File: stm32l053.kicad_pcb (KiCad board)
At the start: 2 copper layers, 29 x 64.5 mm, 5 parts, among them P1 CONN_01X25, P2 CONN_01X25, U1 STM32_LQFP64

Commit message: Restart layout
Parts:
- added C3: 100nF, Capacitors_SMD:C_0805_HandSoldering, B.Cu at (151.8, 116.8)
- added C4: 10uF, Capacitors_SMD:C_0805_HandSoldering, F.Cu at (148.6, 94.0)
- added P3: CONN_01X23, Pin_Headers:Pin_Header_Straight_1x23, F.Cu at (162.6, 81.3)
- added P4: BOOT_MODE, Pin_Headers:Pin_Header_Straight_1x02, F.Cu at (142.2, 81.3)
- added P5: Ext Xtal, Resistors_SMD:R_0805_HandSoldering, F.Cu at (158.8, 110.5)
- added R1: 10K, Resistors_SMD:R_0805_HandSoldering, F.Cu at (174.0, 91.4)
- added R2: 0, Resistors_SMD:R_0805_HandSoldering, F.Cu at (189.2, 100.3)
- added R3: 0, Resistors_SMD:R_0805_HandSoldering, F.Cu at (189.2, 108.0)
- added SW1: SW_PUSH, Buttons_Switches_SMD:SW_SPST_B3U-1000P, F.Cu at (154.9, 81.3)
- C1: moved to B.Cu
- C2: value 100nF -> C
- P1: value CONN_01X25 -> SWD; footprint Pin_Headers:Pin_Header_Straight_1x25 -> Pin_Headers:Pin_Header_Straight_1x06
- P2: value CONN_01X25 -> CONN_01X23; footprint Pin_Headers:Pin_Header_Straight_1x25 -> Pin_Headers:Pin_Header_Straight_1x23
- moved P1 56.2 mm to (143.5, 137.2), turned to 90 degrees
- moved P2 25.4 mm to (137.2, 81.3)
- moved C1 11.8 mm to (148.3, 116.8), turned to 270 degrees
- moved C2 6.52 mm to (142.7, 108.1)
- moved U1 1.27 mm to (149.9, 118.1), turned to 225 degrees
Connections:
- C2 pad 1: VDDA -> Net-(C2-Pad1)
- P1 pad 2: Net-(P1-Pad2) -> SWCLK
- P1 pad 3: Net-(P1-Pad3) -> Earth
- P1 pad 4: Net-(P1-Pad4) -> SWDIO
- P1 pad 5: Net-(P1-Pad5) -> NRST
- P1 pad 6: Net-(P1-Pad6) -> SWO
- P2 pad 1: Net-(P2-Pad1) -> VDD
- P2 pad 10: Net-(P2-Pad10) -> /PA8
- P2 pad 11: Net-(P2-Pad11) -> /PA9
- P2 pad 12: Net-(P2-Pad12) -> /PA10
- P2 pad 13: Net-(P2-Pad13) -> /PA11
- P2 pad 14: Net-(P2-Pad14) -> /PA12
- P2 pad 15: Net-(P2-Pad15) -> /PA15
- P2 pad 16: Net-(P2-Pad16) -> /PC0
- P2 pad 17: Net-(P2-Pad17) -> /PC1
- P2 pad 18: Net-(P2-Pad18) -> /PC2
- P2 pad 19: Net-(P2-Pad19) -> /PC3
- P2 pad 2: Net-(P2-Pad2) -> /PA0
- P2 pad 20: Net-(P2-Pad20) -> /PC4
- P2 pad 21: Net-(P2-Pad21) -> /PC5
- P2 pad 22: Net-(P2-Pad22) -> /PC6
- P2 pad 23: Net-(P2-Pad23) -> Earth
- P2 pad 3: Net-(P2-Pad3) -> /PA1
- P2 pad 4: Net-(P2-Pad4) -> /PA2
- P2 pad 5: Net-(P2-Pad5) -> /PA3
- P2 pad 6: Net-(P2-Pad6) -> /PA4
- P2 pad 7: Net-(P2-Pad7) -> /PA5
- P2 pad 8: Net-(P2-Pad8) -> /PA6
- P2 pad 9: Net-(P2-Pad9) -> /PA7
- U1 pad 1: (no net) -> Net-(C3-Pad2)
- U1 pad 10: Net-(P1-Pad20) -> /PC2
- U1 pad 11: Net-(P1-Pad21) -> /PC3
- U1 pad 12: (no net) -> Earth
- U1 pad 13: VDDA -> VDD
- U1 pad 14: Net-(P1-Pad2) -> /PA0
- U1 pad 15: Net-(P1-Pad3) -> /PA1
- U1 pad 16: Net-(P1-Pad4) -> /PA2
- U1 pad 17: Net-(P1-Pad5) -> /PA3
- U1 pad 18: (no net) -> Earth
- U1 pad 2: Net-(P2-Pad22) -> /PC13
- U1 pad 20: Net-(P1-Pad6) -> /PA4
- U1 pad 21: Net-(P1-Pad7) -> /PA5
- U1 pad 22: Net-(P1-Pad8) -> /PA6
- U1 pad 23: Net-(P1-Pad9) -> /PA7
- U1 pad 24: Net-(P1-Pad22) -> /PC4
- U1 pad 25: Net-(P1-Pad23) -> /PC5
- U1 pad 26: Net-(P2-Pad1) -> /PB0
- U1 pad 27: Net-(P2-Pad2) -> /PB1
- U1 pad 28: Net-(P2-Pad3) -> /PB2
- U1 pad 29: Net-(P2-Pad11) -> /PB10
- U1 pad 3: (no net) -> OSC32_IN
- U1 pad 30: Net-(P2-Pad12) -> /PB11
- U1 pad 31: (no net) -> Earth
- U1 pad 33: Net-(P2-Pad13) -> /PB12
- U1 pad 34: Net-(P2-Pad14) -> /PB13
- U1 pad 35: Net-(P2-Pad15) -> /PB14
- U1 pad 36: Net-(P2-Pad16) -> /PB15
- U1 pad 37: Net-(P1-Pad24) -> /PC6
- U1 pad 38: Net-(P1-Pad25) -> /PC7
- U1 pad 39: Net-(P2-Pad17) -> /PC8
- U1 pad 4: (no net) -> OSC32_OUT
- U1 pad 40: Net-(P2-Pad18) -> /PC9
- U1 pad 41: Net-(P1-Pad10) -> /PA8
- U1 pad 42: Net-(P1-Pad11) -> /PA9
- U1 pad 43: Net-(P1-Pad12) -> /PA10
- U1 pad 44: Net-(P1-Pad13) -> /PA11
- U1 pad 45: Net-(P1-Pad14) -> /PA12
- U1 pad 46: Net-(P1-Pad15) -> SWDIO
- U1 pad 47: (no net) -> Earth
- U1 pad 48: (no net) -> Net-(R3-Pad2)
- U1 pad 49: Net-(P1-Pad16) -> SWCLK
- U1 pad 5: (no net) -> MCO
- U1 pad 50: Net-(P1-Pad17) -> /PA15
- U1 pad 51: Net-(P2-Pad19) -> /PC10
- U1 pad 52: Net-(P2-Pad20) -> /PC11
- U1 pad 53: Net-(P2-Pad21) -> /PC12
- U1 pad 54: (no net) -> /PD2
- U1 pad 55: Net-(P2-Pad4) -> SWO
- U1 pad 56: Net-(P2-Pad5) -> /PB4
- U1 pad 57: Net-(P2-Pad6) -> /PB5
- U1 pad 58: Net-(P2-Pad7) -> /PB6
- U1 pad 59: Net-(P2-Pad8) -> /PB7
- U1 pad 6: (no net) -> Net-(C2-Pad1)
- U1 pad 60: Net-(P2-Pad24) -> BOOT0
- U1 pad 61: Net-(P2-Pad9) -> /PB8
- U1 pad 62: Net-(P2-Pad10) -> /PB9
- U1 pad 63: (no net) -> Earth
- U1 pad 7: Net-(P2-Pad23) -> NRST
- U1 pad 8: Net-(P1-Pad18) -> /PC0
- U1 pad 9: Net-(P1-Pad19) -> /PC1

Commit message: Design rules
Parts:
- added C5: 100nF, Capacitors_SMD:C_0805_HandSoldering, B.Cu at (145.3, 95.2)
- added C6: 100nF, Capacitors_SMD:C_0805_HandSoldering, B.Cu at (147.1, 104.9)
- added C7: 100nF, Capacitors_SMD:C_0805_HandSoldering, B.Cu at (145.3, 113.5)
- P4: value BOOT_MODE -> BOOT0; footprint Pin_Headers:Pin_Header_Straight_1x02 -> Pin_Headers:Pin_Header_Straight_1x01
- P5: footprint Resistors_SMD:R_0805_HandSoldering -> Crystals:Crystal_SMD_0603_2Pads_obsolete
- moved R3 39.9 mm to (149.9, 114.3), turned to 180 degrees
- moved R2 29.5 mm to (160.0, 104.1), turned to 90 degrees
- moved R1 26.8 mm to (149.2, 81.3)
- moved C2 18.0 mm to (154.4, 94.3), turned to 90 degrees
- moved P5 15.3 mm to (157.5, 95.2)
- moved U1 14.0 mm to (149.9, 104.1)
- moved C4 13.7 mm to (141.1, 82.5), turned to 270 degrees
- moved C3 13.5 mm to (152.1, 103.4), turned to 315 degrees
- moved C1 13.4 mm to (158.8, 108.5), turned to 315 degrees
- moved P4 2.54 mm to (144.8, 81.3), turned to 0 degrees
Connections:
- P2 pad 10: /PA8 -> /PA7
- P2 pad 11: /PA9 -> /PA8
- P2 pad 12: /PA10 -> /PA9
- P2 pad 13: /PA11 -> /PA10
- P2 pad 14: /PA12 -> /PA11
- P2 pad 15: /PA15 -> /PA12
- P2 pad 16: /PC0 -> /PA15
- P2 pad 17: /PC1 -> /PC0
- P2 pad 18: /PC2 -> /PC1
- P2 pad 19: /PC3 -> /PC2
- P2 pad 2: /PA0 -> Earth
- P2 pad 20: /PC4 -> /PC3
- P2 pad 21: /PC5 -> /PC4
- P2 pad 22: /PC6 -> /PC5
- P2 pad 23: Earth -> /PC6
- P2 pad 3: /PA1 -> /PA0
- P2 pad 4: /PA2 -> /PA1
- P2 pad 5: /PA3 -> /PA2
- P2 pad 6: /PA4 -> /PA3
- P2 pad 7: /PA5 -> /PA4
- P2 pad 8: /PA6 -> /PA5
- P2 pad 9: /PA7 -> /PA6
- P4 pad 1: VDD -> BOOT0
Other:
- board size 29 x 64.5 mm -> 29 x 59.4 mm
- net class Default: clearance 0.2 -> 0.2032; trace_width 0.25 -> 0.254; via_dia 0.6 -> 0.762; via_drill 0.4 -> 0.4064
- net class Wide added: clearance 0.254, trace_width 0.4064, via_dia 0.762, via_drill 0.4064
- rule trace_clearance: 0.2 -> 0.2032
- rule trace_min: 0.2 -> 0.1524
- rule via_min_drill: 0.3 -> 0.3302
- rule via_min_size: 0.4 -> 0.6858

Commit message: Simpler layout
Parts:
- C2, C4, R1: moved to B.Cu
- moved SW1 56.1 mm to (149.9, 137.2)
- moved P1 55.9 mm to (142.2, 81.3)
- moved R2 20.5 mm to (149.9, 86.4), turned to 180 degrees
- moved R1 20.3 mm to (156.2, 100.3), turned to 315 degrees
- moved P4 12.7 mm to (157.5, 81.3)
- moved C7 12.6 mm to (151.1, 102.4), turned to 315 degrees
- moved C2 12.4 mm to (143.5, 100.3), turned to 225 degrees
- moved C5 9.98 mm to (149.0, 104.5), turned to 315 degrees
- moved P5 8.90 mm to (149.8, 90.7), turned to 0 degrees
- moved C3 7.23 mm to (149.9, 96.5), turned to 180 degrees
- moved C1 6.37 mm to (152.4, 108.0), turned to 45 degrees
- moved R3 4.45 mm to (149.9, 118.7)
- moved C6 1.82 mm to (146.7, 106.7)
- moved C4 1.52 mm to (139.6, 82.5)
- moved U1 1.27 mm to (149.9, 105.4), turned to 315 degrees
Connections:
- net Net-(C3-Pad2) renamed /VLCD
- net Net-(R3-Pad2) renamed /VDD_USB
- P2 pad 10: /PA7 -> /PA2
- P2 pad 11: /PA8 -> /PA3
- P2 pad 12: /PA9 -> /PA4
- P2 pad 13: /PA10 -> /PA5
- P2 pad 14: /PA11 -> /PA6
- P2 pad 15: /PA12 -> /PA7
- P2 pad 16: /PA15 -> /PC4
- P2 pad 17: /PC0 -> /PC5
- P2 pad 18: /PC1 -> /PB0
- P2 pad 19: /PC2 -> /PB1
- P2 pad 20: /PC3 -> /PB2
- P2 pad 21: /PC4 -> /PB10
- P2 pad 22: /PC5 -> /PB11
- P2 pad 23: /PC6 -> /PB12
- P2 pad 3: /PA0 -> /PC13
- P2 pad 4: /PA1 -> /PC0
- P2 pad 5: /PA2 -> /PC1
- P2 pad 6: /PA3 -> /PC2
- P2 pad 7: /PA4 -> /PC3
- P2 pad 8: /PA5 -> /PA0
- P2 pad 9: /PA6 -> /PA1
- P3 pad 1: /PB0 -> /PB9
- P3 pad 10: /PB10 -> /PC10
- P3 pad 11: /PB11 -> /PA15
- P3 pad 12: /PB12 -> /PA12
- P3 pad 13: /PB13 -> /PA11
- P3 pad 14: /PB14 -> /PA10
- P3 pad 15: /PB15 -> /PA9
- P3 pad 16: /PC7 -> /PA8
- P3 pad 17: /PC8 -> /PC9
- P3 pad 18: /PC9 -> /PC8
- P3 pad 19: /PC10 -> /PC7
- P3 pad 2: /PB1 -> /PB8
- P3 pad 20: /PC11 -> /PC6
- P3 pad 21: /PC12 -> /PB15
- P3 pad 22: /PC13 -> /PB14
- P3 pad 23: /PD2 -> /PB13
- P3 pad 3: /PB2 -> /PB7
- P3 pad 4: /PB4 -> /PB6
- P3 pad 6: /PB6 -> /PB4
- P3 pad 7: /PB7 -> /PD2
- P3 pad 8: /PB8 -> /PC12
- P3 pad 9: /PB9 -> /PC11
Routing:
- net /PB12: track 0.00 -> 31.0 mm
- net /PB13: track 0.00 -> 30.1 mm
- net /PB11: track 0.00 -> 27.9 mm
- net /PB14: track 0.00 -> 27.7 mm
- net /PB10: track 0.00 -> 26.0 mm
- net /PC6: track 0.00 -> 23.1 mm
- net /PB2: track 0.00 -> 23.1 mm
- net /PB1: track 0.00 -> 20.7 mm
- net /PC7: track 0.00 -> 20.7 mm
- net /PB8: track 0.00 -> 20.3 mm
- net /PC13: track 0.00 -> 18.4 mm
- net /PC8: track 0.00 -> 18.4 mm
- net /PB0: track 0.15 -> 18.4 mm
- net /PB7: track 0.00 -> 18.2 mm
- net /PB6: track 0.00 -> 16.5 mm
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
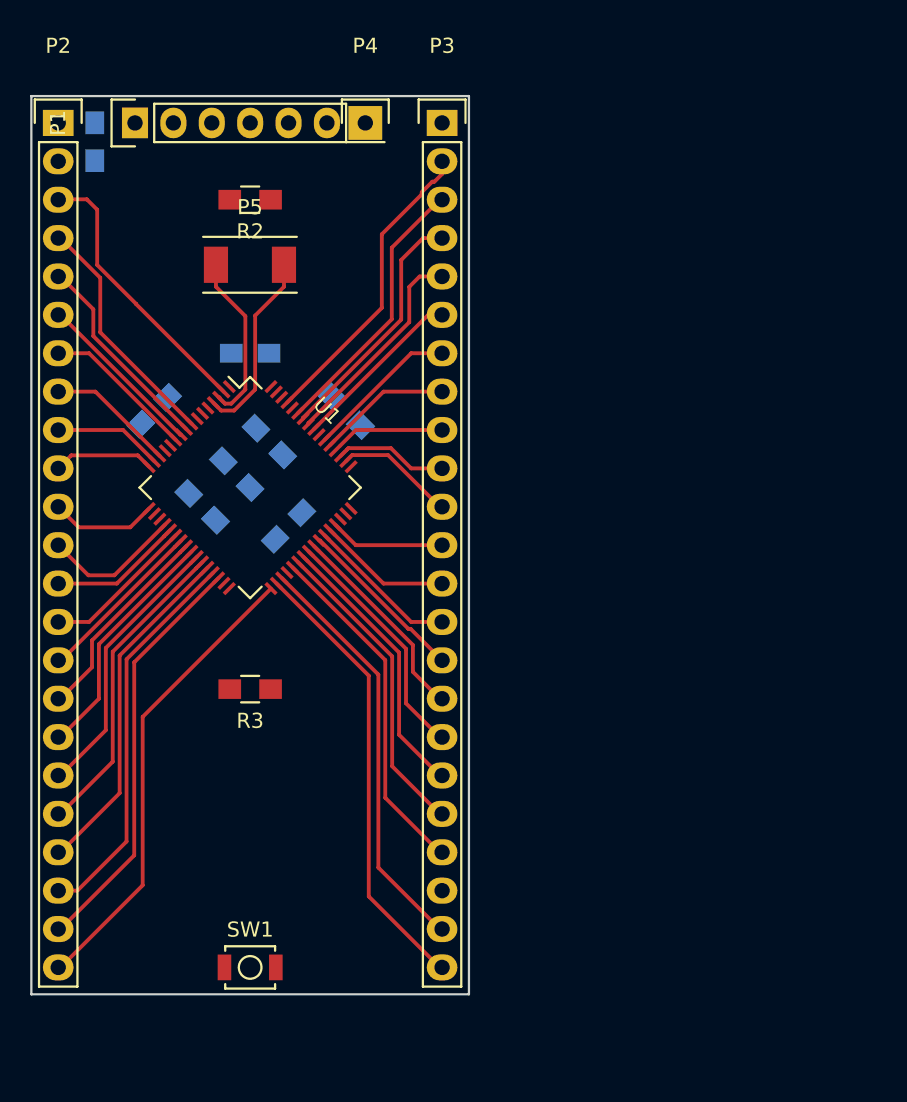
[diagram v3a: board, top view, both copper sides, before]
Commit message: GPIO initial routing
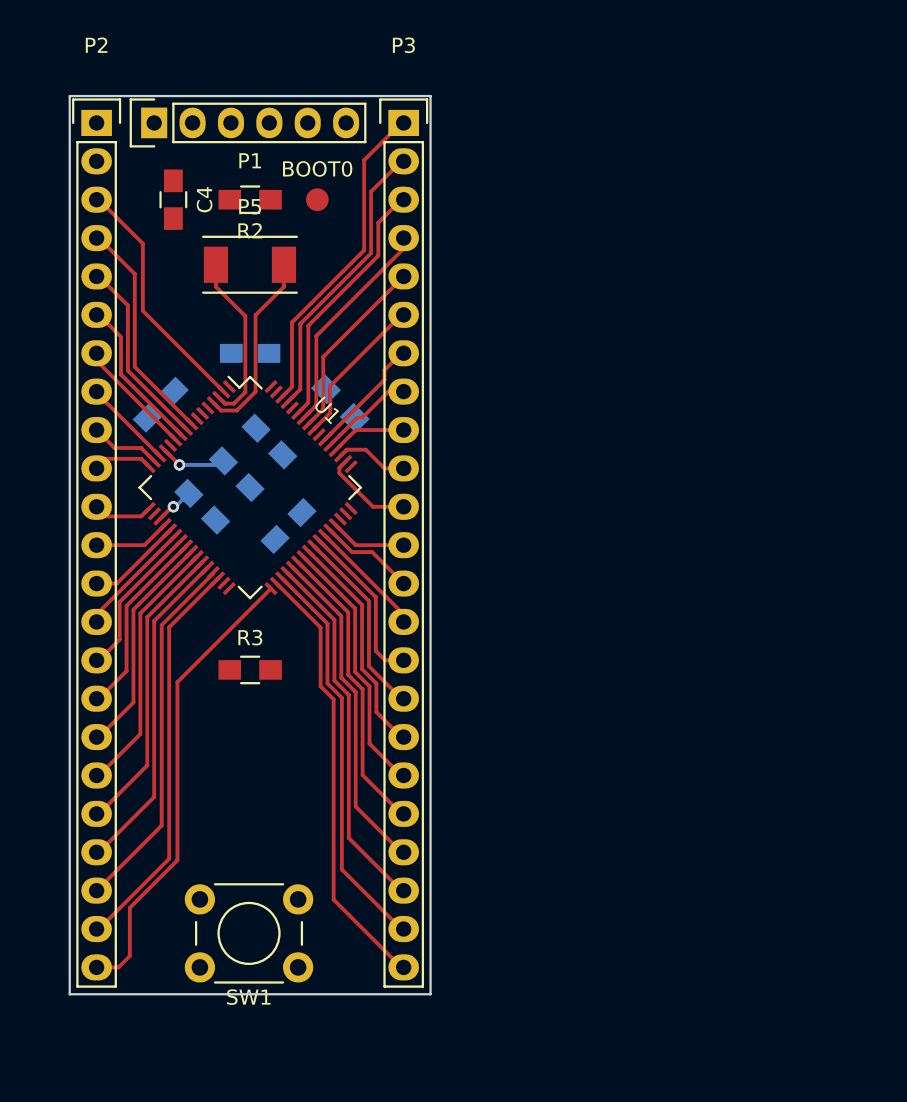
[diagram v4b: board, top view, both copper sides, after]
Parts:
- removed P4: BOOT0, Pin_Headers:Pin_Header_Straight_1x01
- added BOOT0: CONN_01X01, Measurement_Points:Measurement_Point_Round-SMD-Pad_Small, F.Cu at (154.3, 86.4)
- C4: moved to F.Cu
- SW1: value SW_PUSH -> RESET; footprint Buttons_Switches_SMD:SW_SPST_B3U-1000P -> Buttons_Switches_ThroughHole:SW_PUSH_6mm
- moved C4 6.47 mm to (144.8, 86.4)
- moved SW1 3.17 mm to (153.0, 137.2), turned to 180 degrees
- moved P2 2.54 mm to (139.7, 81.3)
- moved P3 2.54 mm to (160.0, 81.3)
- moved R3 1.27 mm to (149.9, 117.5), turned to 0 degrees
- moved P1 1.27 mm to (143.5, 81.3)
- moved R1 0.61 mm to (155.8, 99.8)
- moved C2 0.59 mm to (143.9, 99.9)
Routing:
- net /PB15: track 0.00 -> 24.3 mm
- net /PB9: track 0.15 -> 21.6 mm
- net VDD: track 0.00 -> 6.97 mm, vias 0 -> 2
- net /PA4: track 9.30 -> 5.11 mm
- net /PA3: track 7.10 -> 3.96 mm
- net /PC12: track 8.91 -> 6.09 mm
- net /PA2: track 6.69 -> 3.96 mm
- net /PC10: track 7.50 -> 4.87 mm
- net /PA11: track 8.91 -> 6.37 mm
- net /PA12: track 7.65 -> 5.11 mm
- net /PA1: track 7.23 -> 4.70 mm
- net /PA0: track 8.49 -> 6.00 mm
- net /PC11: track 7.16 -> 4.68 mm
- net /PA6: track 10.2 -> 7.92 mm
- net /PA10: track 10.2 -> 7.92 mm
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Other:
- board size 29 x 59.4 mm -> 23.9 x 59.4 mm

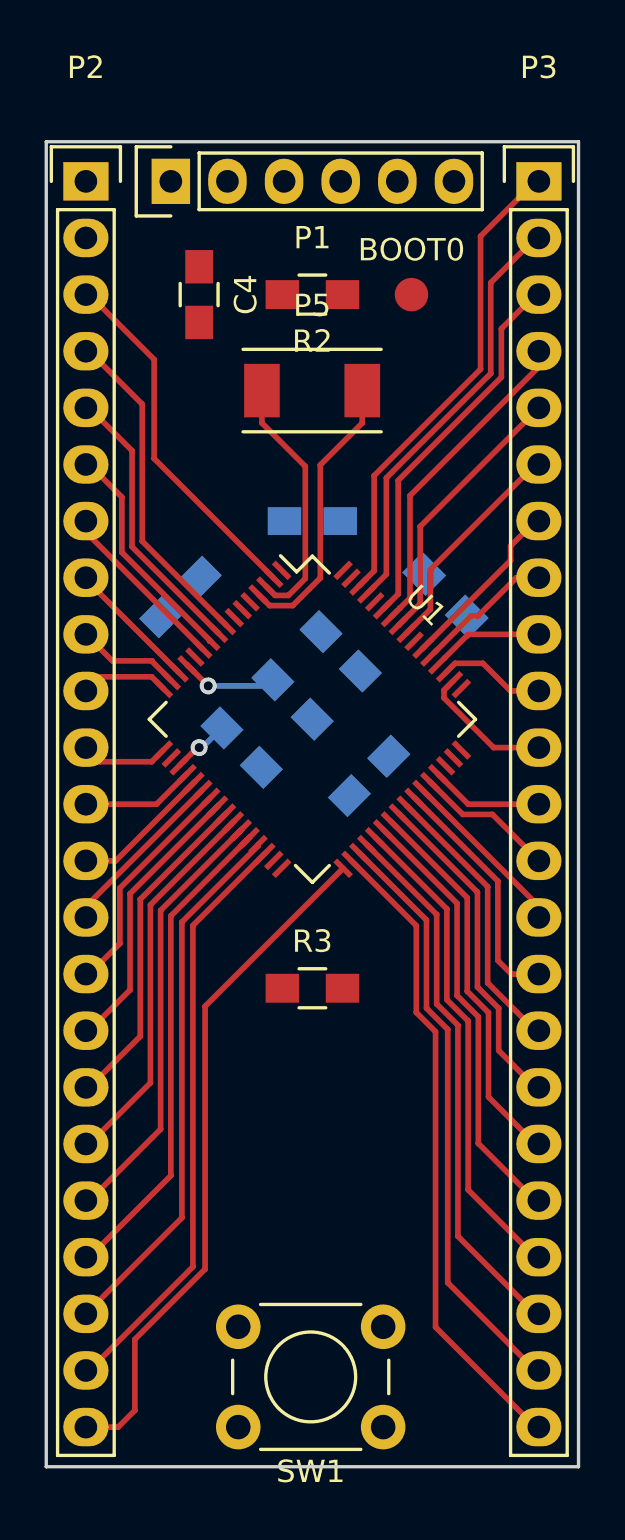
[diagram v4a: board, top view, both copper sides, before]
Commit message: Flipped the headers to the back
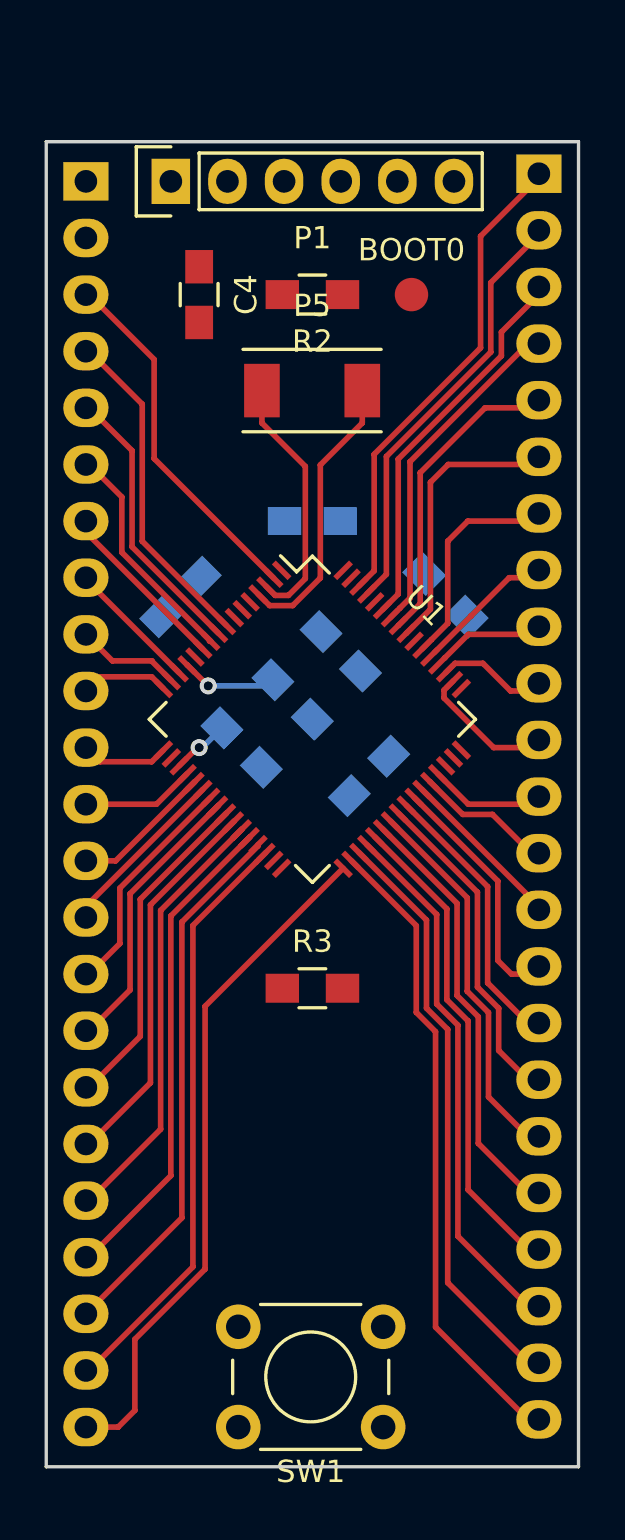
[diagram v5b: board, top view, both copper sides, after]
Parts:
- P2, P3: moved to B.Cu
- moved P3 0.34 mm to (160.0, 80.9), turned to 180 degrees
- turned P2 to 180 degrees
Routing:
- net /PB4: track 10.1 -> 12.4 mm
- net /PD2: track 8.01 -> 9.78 mm
- net /PB5: track 12.4 -> 13.8 mm
